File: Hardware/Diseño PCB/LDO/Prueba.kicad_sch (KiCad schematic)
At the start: 53 parts, among them J1 Vo, Q1 2N3904, Q10 BC557, Q11 BC547, Q12 BC557, Q13 2N3906, Q14 2N3904, Q15 2N3906, Q16 2N3904, Q17 2N3906, Q18 2N3904, Q19 2N3904, Q2 2N3904, Q3 2N3904, Q4 2N3906, Q5 2N3906, Q6 2N3904, Q7 2N3904, Q8 IRF4905, Q9 BC547, U1 TL431LP, U4 LM324

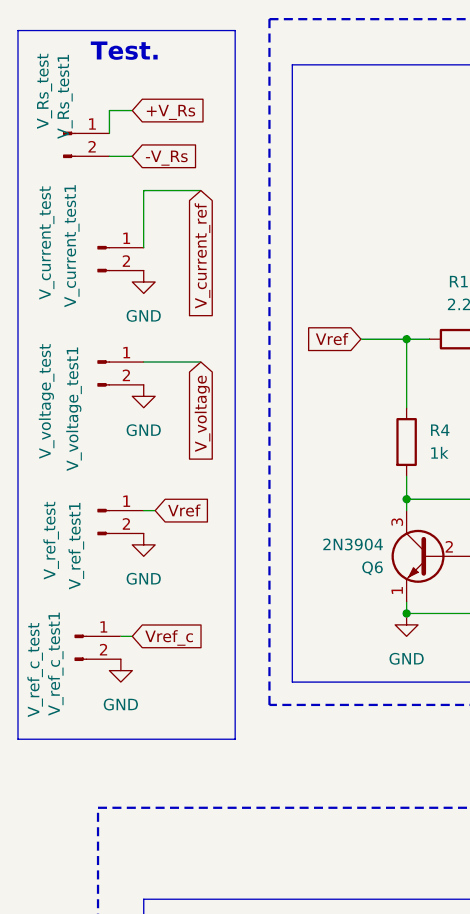
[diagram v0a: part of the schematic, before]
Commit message: Agrupación de modulos en diseño de PCB
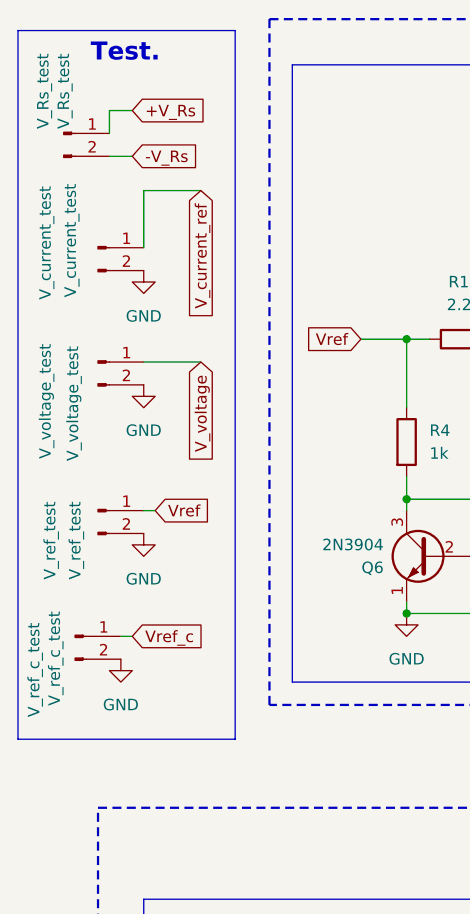
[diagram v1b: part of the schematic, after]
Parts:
- renumbered V_Rs_test1 to V_Rs_test, V_current_test1 to V_current_test, V_ref_c_test1 to V_ref_c_test, V_ref_test1 to V_ref_test, V_voltage_test1 to V_voltage_test
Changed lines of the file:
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@@
 		(in_pos_files yes)
 		(dnp no)
-		(property "Reference" "V_current_test1"
+		(property "Reference" "V_current_test"
 			(at 19.812 32.258 90)
 			(show_name no)
@@
 			(project "Prueba"
 				(path "/70bda0a3-0c17-43ce-af47-54d014630cec"
-					(reference "V_current_test1")
+					(reference "V_current_test")
 					(unit 1)
 				)
@@
 		(in_pos_files yes)
 		(dnp no)
-		(property "Reference" "V_voltage_test1"
+		(property "Reference" "V_voltage_test"
 			(at 20.066 50.292 90)
 			(show_name no)
@@
 			(project "Prueba"
 				(path "/70bda0a3-0c17-43ce-af47-54d014630cec"
-					(reference "V_voltage_test1")
+					(reference "V_voltage_test")
 					(unit 1)
 				)
@@
 		(in_pos_files yes)
 		(dnp no)
-		(property "Reference" "V_ref_c_test1"
+		(property "Reference" "V_ref_c_test"
 			(at 18.034 79.756 90)
 			(show_name no)
@@
 			(project "Prueba"
 				(path "/70bda0a3-0c17-43ce-af47-54d014630cec"
-					(reference "V_ref_c_test1")
+					(reference "V_ref_c_test")
 					(unit 1)
 				)
@@
 		(in_pos_files yes)
 		(dnp no)
-		(property "Reference" "V_Rs_test1"
+		(property "Reference" "V_Rs_test"
 			(at 19.05 17.78 90)
 			(show_name no)
@@
 			(project "Prueba"
 				(path "/70bda0a3-0c17-43ce-af47-54d014630cec"
-					(reference "V_Rs_test1")
+					(reference "V_Rs_test")
 					(unit 1)
 				)
@@
 		(in_pos_files yes)
 		(dnp no)
-		(property "Reference" "V_ref_test1"
+		(property "Reference" "V_ref_test"
 			(at 20.32 67.564 90)
 			(show_name no)
@@
 			(project "Prueba"
 				(path "/70bda0a3-0c17-43ce-af47-54d014630cec"
-					(reference "V_ref_test1")
+					(reference "V_ref_test")
 					(unit 1)
 				)

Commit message: Diseño PCB :  Test con gnd en comun
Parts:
- added GND: Pin_GND, symbol Connector:Conn_01x01_Pin
- Vo1: renamed from J1; footprint Connector_PinHeader_2.00mm:PinHeader_1x01_P2.00mm_Vertical -> Connector_PinHeader_2.00mm:PinHeader_1x02_P2.00mm_Vertical
- renumbered V_Rs_test to V_Rs_test1, V_current_test to V_current_test1, V_ref_c_test to V_ref_c_test1, V_ref_test to V_ref_test1, V_voltage_test to V_voltage_test1
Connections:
- net GND: now also GND.1 (Pin_1)
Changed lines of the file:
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@@
 	(rectangle
 		(start 13.97 15.24)
-		(end 38.1 93.98)
+		(end 38.1 100.33)
 		(stroke
 			(width 0)
@@
 	(wire
 		(pts
+			(xy 27.94 95.25) (xy 33.02 95.25)
+		)
+		(stroke
+			(width 0)
+			(type default)
+		)
+	)
+	(wire
+		(pts
 			(xy 227.33 110.49) (xy 227.33 125.73)
 		)
@@
 		(in_pos_files yes)
 		(dnp no)
-		(property "Reference" "V_current_test"
+		(property "Reference" "V_current_test1"
 			(at 19.812 32.258 90)
 			(show_name no)
@@
 			(project "Prueba"
 				(path "/70bda0a3-0c17-43ce-af47-54d014630cec"
-					(reference "V_current_test")
+					(reference "V_current_test1")
 					(unit 1)
 				)
@@
 	)
 	(symbol
+		(lib_id "Connector:Conn_01x01_Pin")
+		(at 22.86 95.25 0)
+		(unit 1)
+		(body_style 1)
+		(exclude_from_sim no)
+		(in_bom yes)
+		(on_board yes)
+		(in_pos_files yes)
+		(dnp no)
+		(property "Reference" "GND"
+			(at 32.258 93.98 0)
+			(show_name no)
+			(do_not_autoplace no)
+			(effects
+				(font
+					(size 1.27 1.27)
+				)
+			)
+		)
+		(property "Value" "Pin_GND"
+			(at 24.892 97.282 0)
+			(show_name no)
+			(do_not_autoplace no)
+			(effects
+				(font
+					(size 1.27 1.27)
+				)
+			)
+		)
+		(property "Footprint" ""
+			(at 22.86 95.25 0)
+			(hide yes)
+			(show_name no)
+			(do_not_autoplace no)
+			(effects
+				(font
+					(size 1.27 1.27)
+				)
+			)
+		)
+		(property "Datasheet" ""
+			(at 22.86 95.25 0)
+			(hide yes)
+			(show_name no)
+			(do_not_autoplace no)
+			(effects
+				(font
+					(size 1.27 1.27)
+				)
+			)
+		)
+		(property "Description" "Generic connector, single row, 01x01, script generated"
+			(at 22.86 95.25 0)
+			(hide yes)
+			(show_name no)
+			(do_not_autoplace no)
+			(effects
+				(font
+					(size 1.27 1.27)
+				)
+			)
+		)
+		(pin "1"
+		)
+		(instances
+			(project "Prueba"
+				(path "/70bda0a3-0c17-43ce-af47-54d014630cec"
+					(reference "GND")
+					(unit 1)
+				)
+			)
+		)
+	)
+	(symbol
 		(lib_id "Device:R")
 		(at 63.5 49.53 90)
@@
 		(in_pos_files yes)
 		(dnp no)
-		(property "Reference" "J1"
+		(property "Reference" "Vo1"
 			(at 266.192 151.13 0)
 			(show_name no)
@@
 			)
 		)
-		(property "Footprint" "Connector_PinHeader_2.00mm:PinHeader_1x01_P2.00mm_Vertical"
+		(property "Footprint" "Connector_PinHeader_2.00mm:PinHeader_1x02_P2.00mm_Vertical"
 			(at 265.43 151.13 0)
 			(hide yes)
@@
 			(project "Prueba"
 				(path "/70bda0a3-0c17-43ce-af47-54d014630cec"
-					(reference "J1")
+					(reference "Vo1")
 					(unit 1)
 				)
@@
 	(symbol
 		(lib_id "power:GND")
+		(at 33.02 95.25 0)
+		(unit 1)
+		(body_style 1)
+		(exclude_from_sim no)
+		(in_bom yes)
+		(on_board yes)
+		(in_pos_files yes)
+		(dnp no)
+		(property "Reference" "#PWR022"
+			(at 33.02 101.6 0)
+			(hide yes)
+			(show_name no)
+			(do_not_autoplace no)
+			(effects
+				(font
+					(size 1.27 1.27)
+				)
+			)
+		)
+		(property "Value" "GND"
+			(at 32.258 93.98 0)
+			(show_name no)
+			(do_not_autoplace no)
+			(effects
+				(font
+					(size 1.27 1.27)
+				)
+			)
+		)
+		(property "Footprint" ""
+			(at 33.02 95.25 0)
+			(hide yes)
+			(show_name no)
+			(do_not_autoplace no)
+			(effects
+				(font
+					(size 1.27 1.27)
+				)
+			)
+		)
+		(property "Datasheet" ""
+			(at 33.02 95.25 0)
+			(hide yes)
+			(show_name no)
+			(do_not_autoplace no)
+			(effects
+				(font
+					(size 1.27 1.27)
+				)
+			)
+		)
+		(property "Description" "Power symbol creates a global label with name \"GND\" , ground"
+			(at 33.02 95.25 0)
+			(hide yes)
+			(show_name no)
+			(do_not_autoplace no)
+			(effects
+				(font
+					(size 1.27 1.27)
+				)
+			)
+		)
+		(pin "1"
+		)
+		(instances
+			(project "Prueba"
+				(path "/70bda0a3-0c17-43ce-af47-54d014630cec"
+					(reference "#PWR022")
+					(unit 1)
+				)
+			)
+		)
+	)
+	(symbol
+		(lib_id "power:GND")
 		(at 25.4 85.09 0)
 		(unit 1)
@@
 		(in_pos_files yes)
 		(dnp no)
-		(property "Reference" "V_voltage_test"
+		(property "Reference" "V_voltage_test1"
 			(at 20.066 50.292 90)
 			(show_name no)
@@
 			(project "Prueba"
 				(path "/70bda0a3-0c17-43ce-af47-54d014630cec"
-					(reference "V_voltage_test")
+					(reference "V_voltage_test1")
 					(unit 1)
 				)
@@
 		(in_pos_files yes)
 		(dnp no)
-		(property "Reference" "V_ref_c_test"
+		(property "Reference" "V_ref_c_test1"
 			(at 18.034 79.756 90)
 			(show_name no)
@@
 			(project "Prueba"
 				(path "/70bda0a3-0c17-43ce-af47-54d014630cec"
-					(reference "V_ref_c_test")
+					(reference "V_ref_c_test1")
 					(unit 1)
 				)
@@
 		(in_pos_files yes)
 		(dnp no)
-		(property "Reference" "V_Rs_test"
+		(property "Reference" "V_Rs_test1"
 			(at 19.05 17.78 90)
 			(show_name no)
@@
 			(project "Prueba"
 				(path "/70bda0a3-0c17-43ce-af47-54d014630cec"
-					(reference "V_Rs_test")
+					(reference "V_Rs_test1")
 					(unit 1)
 				)
@@
 		(in_pos_files yes)
 		(dnp no)
-		(property "Reference" "V_ref_test"
+		(property "Reference" "V_ref_test1"
 			(at 20.32 67.564 90)
 			(show_name no)
@@
 			(project "Prueba"
 				(path "/70bda0a3-0c17-43ce-af47-54d014630cec"
-					(reference "V_ref_test")
+					(reference "V_ref_test1")
 					(unit 1)
 				)

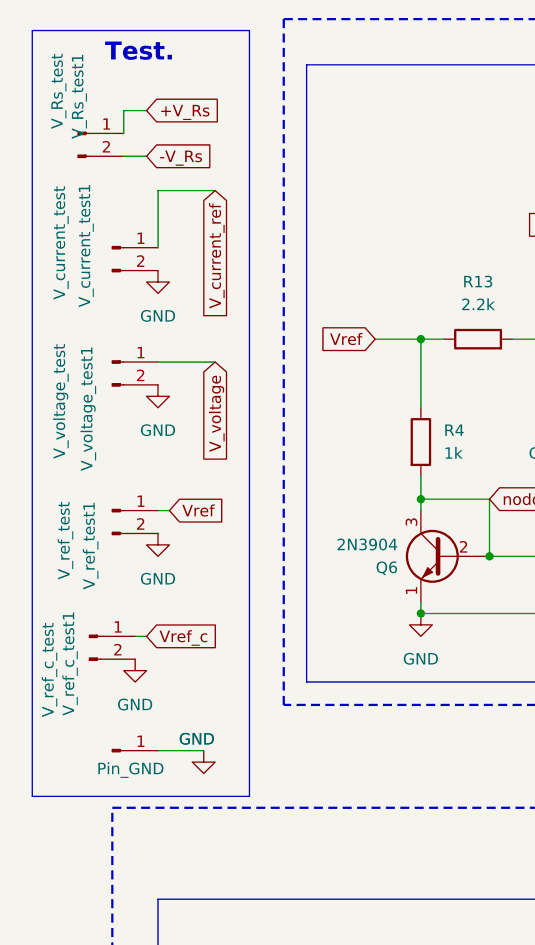
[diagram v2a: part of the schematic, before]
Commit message: Diseño PCB: Indicador de operacionales dentro de encapsulado
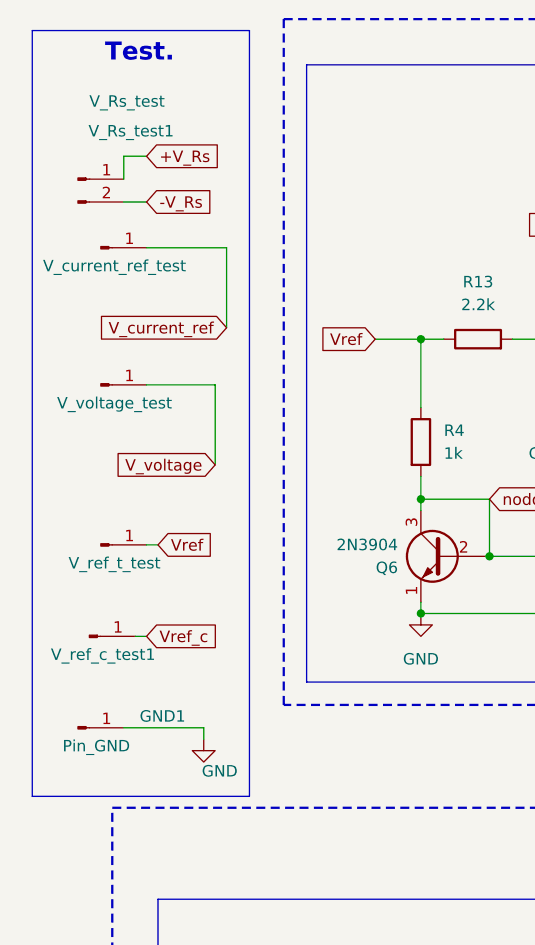
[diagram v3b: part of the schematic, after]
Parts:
- removed V_current_test1: V_current_test, Connector_PinHeader_2.00mm:PinHeader_1x01_P2.00mm_Vertical, symbol Connector:Conn_01x02_Pin
- removed V_ref_c_test1: V_ref_c_test, Connector_PinHeader_2.00mm:PinHeader_1x01_P2.00mm_Vertical, symbol Connector:Conn_01x02_Pin
- removed V_ref_test1: V_ref_test, Connector_PinHeader_2.00mm:PinHeader_1x01_P2.00mm_Vertical, symbol Connector:Conn_01x02_Pin
- removed V_voltage_test1: V_voltage_test, Connector_PinHeader_2.00mm:PinHeader_1x01_P2.00mm_Vertical, symbol Connector:Conn_01x02_Pin
- added GND2: V_ref_c_test1, Connector_PinHeader_2.00mm:PinHeader_1x01_P2.00mm_Vertical, symbol Connector:Conn_01x01_Pin
- added GND3: V_ref_t_test, Connector_PinHeader_2.00mm:PinHeader_1x01_P2.00mm_Vertical, symbol Connector:Conn_01x01_Pin
- added GND4: V_voltage_test, Connector_PinHeader_2.00mm:PinHeader_1x01_P2.00mm_Vertical, symbol Connector:Conn_01x01_Pin
- added GND5: V_current_ref_test, Connector_PinHeader_2.00mm:PinHeader_1x01_P2.00mm_Vertical, symbol Connector:Conn_01x01_Pin
- GND1: renamed from GND; footprint (none) -> Connector_PinHeader_2.00mm:PinHeader_1x01_P2.00mm_Vertical
- V_Rs_test1: footprint Connector_PinHeader_2.00mm:PinHeader_1x01_P2.00mm_Vertical -> Connector_PinHeader_2.00mm:PinHeader_1x02_P2.00mm_Vertical
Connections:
- net V_current_ref: now also GND5.1 (Pin_1)
- net V_voltage: now also GND4.1 (Pin_1)
- net Vref: now also GND3.1 (Pin_1)
- net Vref_c: now also GND2.1 (Pin_1)
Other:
- moved on the sheet: GND1, V_Rs_test1

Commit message: Diseño PCB
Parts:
- U4: footprint Package_DIP:DIP-16_W10.16mm_LongPads -> Package_DIP:DIP-14_W10.16mm_LongPads
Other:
- moved on the sheet: Q1, R1, R2, U1
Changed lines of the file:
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@@
 	)
 	(junction
-		(at 140.97 135.89)
+		(at 143.51 135.89)
 		(diameter 0)
 		(color 0 0 0 0)
@@
 	)
 	(junction
-		(at 140.97 115.57)
+		(at 143.51 115.57)
 		(diameter 0)
 		(color 0 0 0 0)
@@
 	)
 	(junction
-		(at 156.21 128.27)
+		(at 128.27 128.27)
 		(diameter 0)
 		(color 0 0 0 0)
@@
 	)
 	(junction
-		(at 140.97 146.05)
+		(at 143.51 146.05)
 		(diameter 0)
 		(color 0 0 0 0)
@@
 	(wire
 		(pts
-			(xy 140.97 133.35) (xy 140.97 135.89)
+			(xy 143.51 133.35) (xy 143.51 135.89)
 		)
 		(stroke
@@
 	(wire
 		(pts
-			(xy 140.97 115.57) (xy 132.08 115.57)
+			(xy 143.51 115.57) (xy 152.4 115.57)
 		)
 		(stroke
@@
 	(wire
 		(pts
-			(xy 153.67 146.05) (xy 140.97 146.05)
+			(xy 130.81 146.05) (xy 143.51 146.05)
 		)
 		(stroke
@@
 	(wire
 		(pts
-			(xy 148.59 128.27) (xy 156.21 128.27)
+			(xy 135.89 128.27) (xy 128.27 128.27)
 		)
 		(stroke
@@
 	(wire
 		(pts
-			(xy 156.21 118.11) (xy 156.21 115.57)
+			(xy 128.27 118.11) (xy 128.27 115.57)
 		)
 		(stroke
@@
 	(wire
 		(pts
-			(xy 156.21 125.73) (xy 156.21 128.27)
+			(xy 128.27 125.73) (xy 128.27 128.27)
 		)
 		(stroke
@@
 	(wire
 		(pts
-			(xy 140.97 115.57) (xy 140.97 123.19)
+			(xy 143.51 115.57) (xy 143.51 123.19)
 		)
 		(stroke
@@
 	(wire
 		(pts
-			(xy 156.21 115.57) (xy 140.97 115.57)
+			(xy 128.27 115.57) (xy 143.51 115.57)
 		)
 		(stroke
@@
 	(wire
 		(pts
-			(xy 140.97 135.89) (xy 140.97 146.05)
+			(xy 143.51 135.89) (xy 143.51 146.05)
 		)
 		(stroke
@@
 	(wire
 		(pts
-			(xy 132.08 135.89) (xy 140.97 135.89)
+			(xy 152.4 135.89) (xy 143.51 135.89)
 		)
 		(stroke
@@
 	(wire
 		(pts
-			(xy 156.21 128.27) (xy 156.21 143.51)
+			(xy 128.27 128.27) (xy 128.27 143.51)
 		)
 		(stroke
@@
 	(global_label "Vref"
 		(shape input)
-		(at 132.08 135.89 180)
+		(at 152.4 135.89 0)
 		(fields_autoplaced yes)
 		(effects
@@
 				(size 1.27 1.27)
 			)
-			(justify right)
+			(justify left)
 		)
 		(property "Intersheetrefs" "${INTERSHEET_REFS}"
-			(at 125.4057 135.89 0)
+			(at 159.0743 135.89 0)
 			(hide yes)
 			(show_name no)
@@
 					(size 1.27 1.27)
 				)
-				(justify right)
+				(justify left)
 			)
 		)
@@
 	(global_label "Vcc"
 		(shape input)
-		(at 132.08 115.57 180)
+		(at 152.4 115.57 0)
 		(fields_autoplaced yes)
 		(effects
@@
 				(size 1.27 1.27)
 			)
-			(justify right)
+			(justify left)
 		)
 		(property "Intersheetrefs" "${INTERSHEET_REFS}"
-			(at 125.829 115.57 0)
+			(at 158.651 115.57 0)
 			(hide yes)
 			(show_name no)
@@
 					(size 1.27 1.27)
 				)
-				(justify right)
+				(justify left)
 			)
 		)
@@
 			)
 		)
-		(property "Footprint" "Package_DIP:DIP-16_W10.16mm_LongPads"
+		(property "Footprint" "Package_DIP:DIP-14_W10.16mm_LongPads"
 			(at 260.35 20.32 0)
 			(hide yes)
@@
 			)
 		)
-		(property "Footprint" "Package_DIP:DIP-16_W10.16mm_LongPads"
+		(property "Footprint" "Package_DIP:DIP-14_W10.16mm_LongPads"
 			(at 260.35 52.07 0)
 			(hide yes)
@@
 	(symbol
 		(lib_id "Device:R")
-		(at 156.21 121.92 0)
+		(at 128.27 121.92 0)
+		(mirror y)
 		(unit 1)
 		(body_style 1)
@@
 		(dnp no)
 		(property "Reference" "R1"
-			(at 150.876 121.158 0)
+			(at 133.604 121.158 0)
 			(show_name no)
 			(do_not_autoplace no)
@@
 		)
 		(property "Value" "2.2k"
-			(at 150.622 123.444 0)
+			(at 133.858 123.444 0)
 			(show_name no)
 			(do_not_autoplace no)
@@
 		)
 		(property "Footprint" "Resistor_THT:R_Axial_DIN0204_L3.6mm_D1.6mm_P7.62mm_Horizontal"
-			(at 154.432 121.92 90)
+			(at 130.048 121.92 90)
 			(hide yes)
 			(show_name no)
@@
 		)
 		(property "Datasheet" ""
-			(at 156.21 121.92 0)
+			(at 128.27 121.92 0)
 			(hide yes)
 			(show_name no)
@@
 		)
 		(property "Description" "Resistor"
-			(at 156.21 121.92 0)
+			(at 128.27 121.92 0)
 			(hide yes)
 			(show_name no)
@@
 	(symbol
 		(lib_id "Transistor_BJT:2N3904")
-		(at 143.51 128.27 0)
-		(mirror y)
+		(at 140.97 128.27 0)
 		(unit 1)
 		(body_style 1)
@@
 		(dnp no)
 		(property "Reference" "Q1"
-			(at 138.43 129.5401 0)
+			(at 146.05 129.5401 0)
 			(show_name no)
 			(do_not_autoplace no)
@@
 		)
 		(property "Value" "2N3904"
-			(at 138.43 127.0001 0)
+			(at 146.05 127.0001 0)
 			(show_name no)
 			(do_not_autoplace no)
@@
 		)
 		(property "Footprint" "Package_TO_SOT_THT:TO-92_Inline"
-			(at 138.43 130.175 0)
+			(at 146.05 130.175 0)
 			(hide yes)
 			(show_name no)
@@
 		)
 		(property "Datasheet" "https://www.onsemi.com/pub/Collateral/2N3903-D.PDF"
-			(at 143.51 128.27 0)
+			(at 140.97 128.27 0)
 			(hide yes)
 			(show_name no)
@@
 		)
 		(property "Description" "0.2A Ic, 40V Vce, Small Signal NPN Transistor, TO-92"
-			(at 143.51 128.27 0)
+			(at 140.97 128.27 0)
 			(hide yes)
 			(show_name no)
@@
 			)
 		)
-		(property "Footprint" "Package_DIP:DIP-16_W10.16mm_LongPads"
+		(property "Footprint" "Package_DIP:DIP-14_W10.16mm_LongPads"
 			(at 85.09 163.83 0)
 			(hide yes)
@@
 	(symbol
 		(lib_id "power:GND")
-		(at 156.21 148.59 0)
+		(at 128.27 148.59 0)
+		(mirror y)
 		(unit 1)
 		(body_style 1)
@@
 		(fields_autoplaced yes)
 		(property "Reference" "#PWR02"
-			(at 156.21 154.94 0)
+			(at 128.27 154.94 0)
 			(hide yes)
 			(show_name no)
@@
 		)
 		(property "Value" "GND"
-			(at 156.21 153.67 0)
+			(at 128.27 153.67 0)
 			(show_name no)
 			(do_not_autoplace no)
@@
 		)
 		(property "Footprint" ""
-			(at 156.21 148.59 0)
+			(at 128.27 148.59 0)
 			(hide yes)
 			(show_name no)
@@
 		)
 		(property "Datasheet" ""
-			(at 156.21 148.59 0)
+			(at 128.27 148.59 0)
 			(hide yes)
 			(show_name no)
@@
 		)
 		(property "Description" "Power symbol creates a global label with name \"GND\" , ground"
-			(at 156.21 148.59 0)
+			(at 128.27 148.59 0)
 			(hide yes)
 			(show_name no)
@@
 	(symbol
 		(lib_id "power:GND")
-		(at 140.97 153.67 0)
+		(at 143.51 153.67 0)
+		(mirror y)
 		(unit 1)
 		(body_style 1)
@@
 		(fields_autoplaced yes)
 		(property "Reference" "#PWR01"
-			(at 140.97 160.02 0)
+			(at 143.51 160.02 0)
 			(hide yes)
 			(show_name no)
@@
 		)
 		(property "Value" "GND"
-			(at 140.97 158.75 0)
+			(at 143.51 158.75 0)
 			(show_name no)
 			(do_not_autoplace no)
@@
 		)
 		(property "Footprint" ""
-			(at 140.97 153.67 0)
+			(at 143.51 153.67 0)
 			(hide yes)
 			(show_name no)
@@
 		)
 		(property "Datasheet" ""
-			(at 140.97 153.67 0)
+			(at 143.51 153.67 0)
 			(hide yes)
 			(show_name no)
@@
 		)
 		(property "Description" "Power symbol creates a global label with name \"GND\" , ground"
-			(at 140.97 153.67 0)
+			(at 143.51 153.67 0)
 			(hide yes)
 			(show_name no)
@@
 			)
 		)
-		(property "Footprint" "Package_DIP:DIP-16_W10.16mm_LongPads"
+		(property "Footprint" "Package_DIP:DIP-14_W10.16mm_LongPads"
 			(at 41.91 139.7 0)
 			(hide yes)
@@
 			)
 		)
-		(property "Footprint" "Package_DIP:DIP-16_W10.16mm_LongPads"
+		(property "Footprint" "Package_DIP:DIP-14_W10.16mm_LongPads"
 			(at 83.82 132.08 0)
 			(hide yes)
@@
 	(symbol
 		(lib_id "Reference_Voltage:TL431LP")
-		(at 156.21 146.05 90)
+		(at 128.27 146.05 270)
+		(mirror x)
 		(unit 1)
 		(body_style 1)
@@
 		(dnp no)
 		(property "Reference" "U1"
-			(at 153.162 142.494 90)
+			(at 131.318 142.494 90)
 			(show_name no)
 			(do_not_autoplace no)
@@
 		)
 		(property "Value" "TL431LP"
-			(at 147.828 148.082 90)
+			(at 136.652 148.082 90)
 			(show_name no)
 			(do_not_autoplace no)
@@
 		)
 		(property "Footprint" "Package_TO_SOT_THT:TO-92_Inline"
-			(at 161.036 146.05 0)
+			(at 123.444 146.05 0)
 			(hide yes)
 			(show_name no)
@@
 		)
 		(property "Datasheet" "http://www.ti.com/lit/ds/symlink/tl431.pdf"
-			(at 163.322 145.542 0)
+			(at 121.158 145.542 0)
 			(hide yes)
 			(show_name no)
@@
 		)
 		(property "Description" "Shunt Regulator, TO-92"
-			(at 165.1 146.05 0)
+			(at 119.38 146.05 0)
 			(hide yes)
 			(show_name no)
@@
 	(symbol
 		(lib_id "Device:R")
-		(at 140.97 149.86 0)
+		(at 143.51 149.86 0)
+		(mirror y)
 		(unit 1)
 		(body_style 1)
@@
 		(fields_autoplaced yes)
 		(property "Reference" "R2"
-			(at 143.51 148.5899 0)
+			(at 140.97 148.5899 0)
 			(show_name no)
 			(do_not_autoplace no)
@@
 		)
 		(property "Value" "10k"
-			(at 143.51 151.1299 0)
+			(at 140.97 151.1299 0)
 			(show_name no)
 			(do_not_autoplace no)
@@
 		)
 		(property "Footprint" "Resistor_THT:R_Axial_DIN0204_L3.6mm_D1.6mm_P7.62mm_Horizontal"
-			(at 139.192 149.86 90)
+			(at 145.288 149.86 90)
 			(hide yes)
 			(show_name no)
@@
 		)
 		(property "Datasheet" ""
-			(at 140.97 149.86 0)
+			(at 143.51 149.86 0)
 			(hide yes)
 			(show_name no)
@@
 		)
 		(property "Description" "Resistor"
-			(at 140.97 149.86 0)
+			(at 143.51 149.86 0)
 			(hide yes)
 			(show_name no)

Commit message: PCB: Diseño
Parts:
- added V_in1: Vin, Connector_PinHeader_2.00mm:PinHeader_1x02_P2.00mm_Vertical, symbol Connector:Conn_01x02_Pin
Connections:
- net GND: now also V_in1.2 (Pin_2)
- net Vcc: now also V_in1.1 (Pin_1)
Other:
- note added: "Señal de Entrada"
- moved on the sheet: Q1, Q10, Q11, Q12, Q13, Q19, Q8, Q9, R1, R10, R11, R12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
